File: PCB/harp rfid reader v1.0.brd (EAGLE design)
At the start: 37.5 x 26.5 mm, 38 parts, among them IC1 FT232RL, IC2 LP5907MFX-3.3, IC3 ATXMEGAxxxA4U-AU, Q1 BC817-40W, U1 ID-12/20SMD

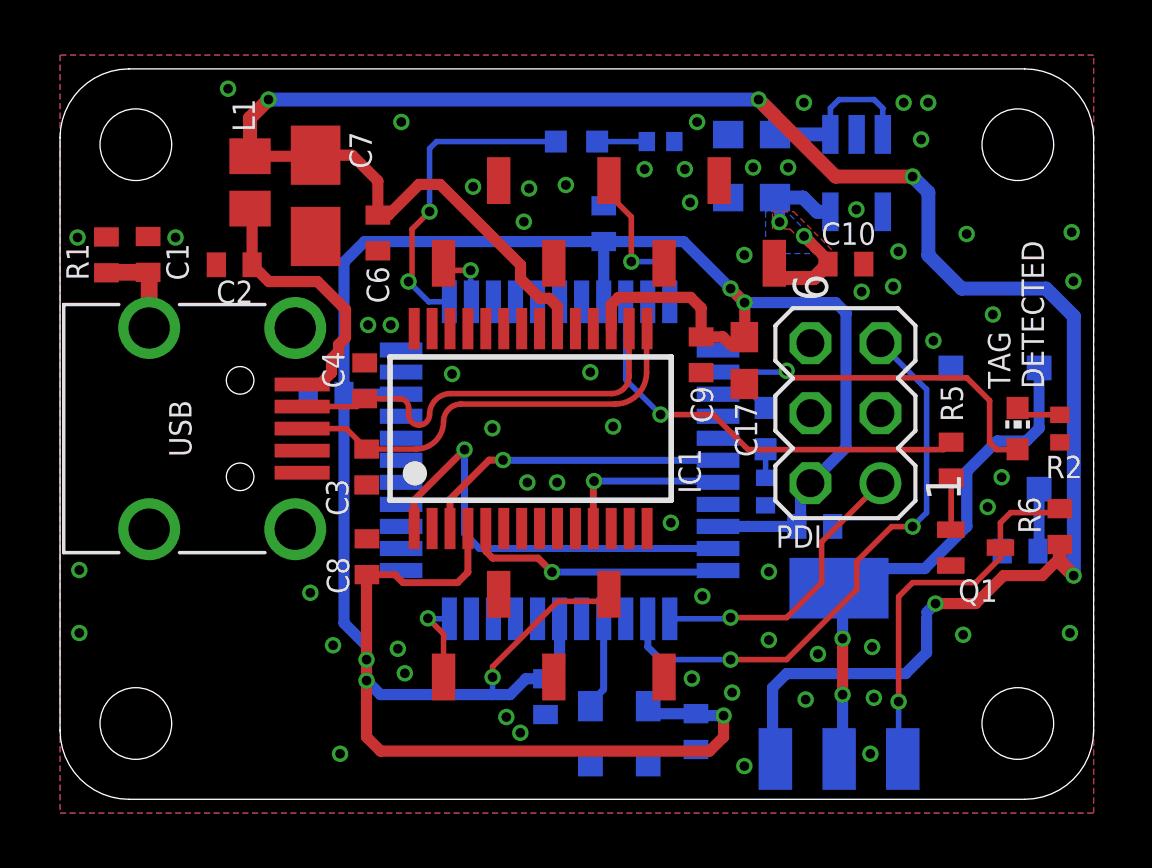
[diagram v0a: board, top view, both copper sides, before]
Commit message: Increased oscillator and buzzer pads.
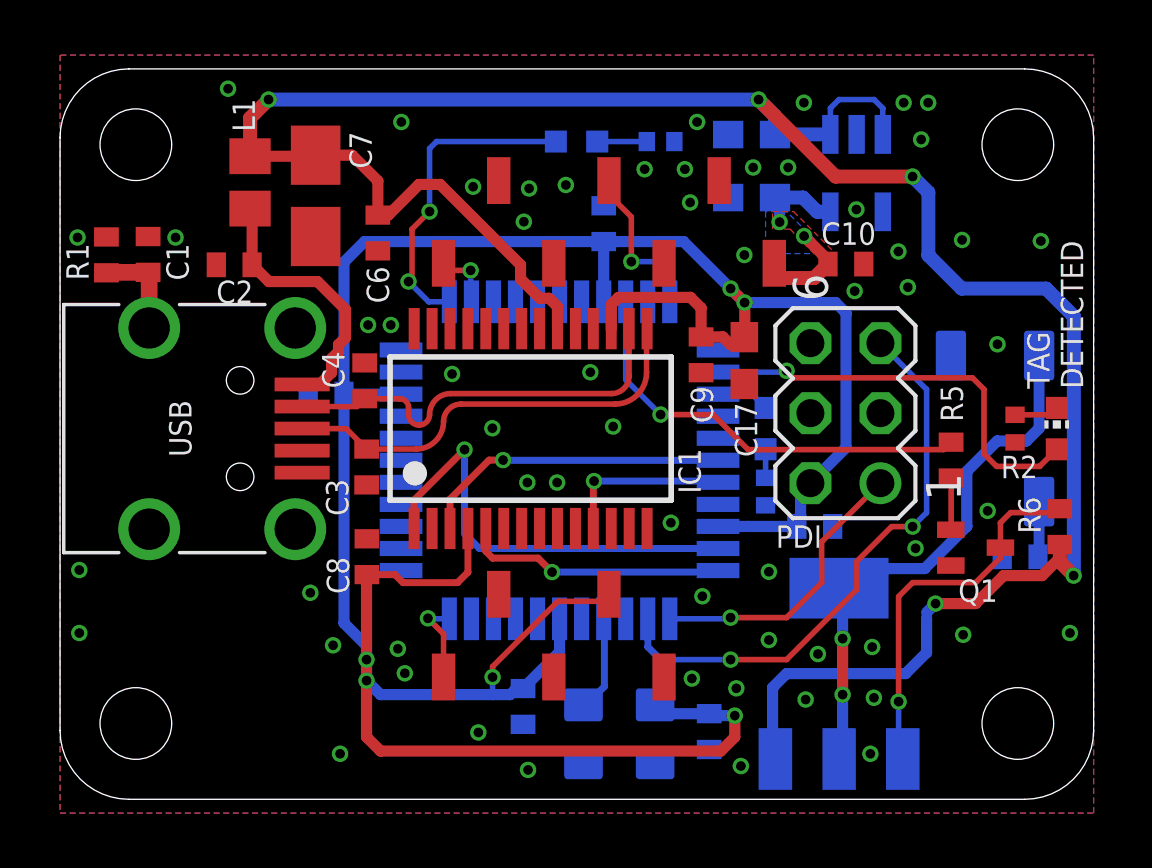
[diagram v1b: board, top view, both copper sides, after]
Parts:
- OSC1: value (none) -> CNP-MISCELLANEOUS_OSCILLATOR; device CNP-miscellaneous:OSCILLATOR_3.2X2.5 -> harp rfid reader v1.0:CNP-MISCELLANEOUS_OSCILLATOR_3.2X2.5
- SP1: value SMT-0540-S-R -> BUZZER-COIL_SMT-0540-S-R; device Buzzer Coil:SMT-0540-S-R -> harp rfid reader v1.0:BUZZER-COIL_SMT-0540-S-R
- moved R2 1.63 mm to (34.6, 13.4)
- moved TAG_T 1.42 mm to (36.2, 13.4)
- moved C16 0.89 mm to (16.8, 3.37)
- moved C12 0.48 mm to (23.6, 2.46)
- moved R7 0.20 mm to (34.8, 8.80)
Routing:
- net DETECT2: track 13.0 -> 15.4 mm
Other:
- board text added: "125 KHz"
- board text added: "DATA"
- board text added: "GND"
- board text added: "PDI"
- board text added: "VCC"
